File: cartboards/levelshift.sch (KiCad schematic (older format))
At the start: 2 parts, among them J1 CES-106-01-T-S, J2 CES-106-01-T-S

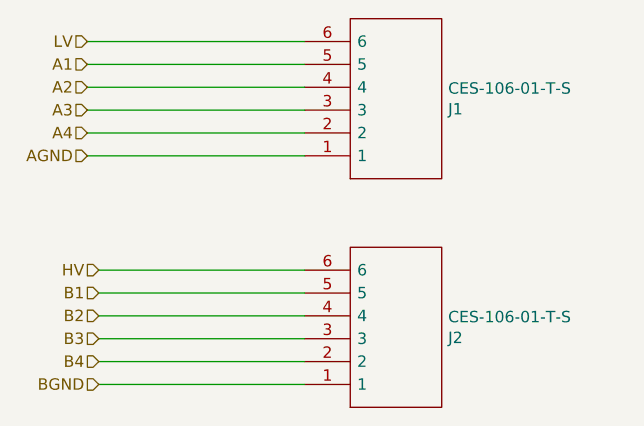
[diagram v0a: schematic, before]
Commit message: Tweak trace width for power in schematics
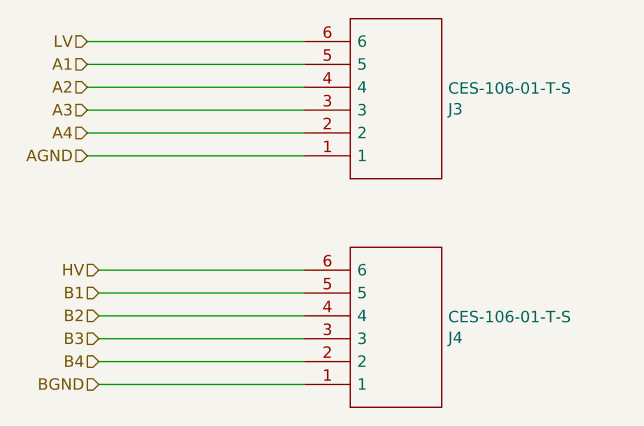
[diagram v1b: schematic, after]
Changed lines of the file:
@@
 $Descr A4 11693 8268
 encoding utf-8
-Sheet 2 4
+Sheet 3 4
 Title ""
 Date ""
@@
 AR Path="/619C8BAD/619B34A6" Ref="J2"  Part="1"
 AR Path="/619D5859/619B34A6" Ref="J4"  Part="1"
-F 0 "J2" H 5628 3796 50  0000 L CNN
+F 0 "J4" H 5628 3796 50  0000 L CNN
 F 1 "CES-106-01-T-S" H 5628 3705 50  0000 L CNN
 F 2 "CES-106-XX-Y-S" H 5650 4100 50  0001 L CNN
@@
 AR Path="/619C8BAD/619B29BD" Ref="J1"  Part="1"
 AR Path="/619D5859/619B29BD" Ref="J3"  Part="1"
-F 0 "J1" H 5628 2796 50  0000 L CNN
+F 0 "J3" H 5628 2796 50  0000 L CNN
 F 1 "CES-106-01-T-S" H 5628 2705 50  0000 L CNN
 F 2 "CES-106-XX-Y-S" H 5650 3100 50  0001 L CNN
